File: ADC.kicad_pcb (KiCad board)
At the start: 2 copper layers, 195 parts, among them J1 Conn_01x03_Pin, J2 Screw_Terminal_01x02, J3 Screw_Terminal_01x09, SW1 SW_SPDT, U1 ADS1256IDBR, U10 CD4514BM, U11 ADG5412FBCPZ-RL7, U12 ADR421ARMZ, U13 OPA211ID, U14 ADG5412FBCPZ-RL7, U15 OPA211ID, U16 ADG5412FBCPZ-RL7, U17 OPA211ID, U18 CD4072BM, U19 CD4514BM, U2 MCU-STM32F407VET6_LQFP100_, U20 ADG5412FBCPZ-RL7, U21 ADG5412FBCPZ-RL7, U22 ADG5412FBCPZ-RL7, U23 ADG5412FBCPZ-RL7, U24 OPA211ID, U25 OPA211ID, U26 OPA211ID, U27 OPA211ID, U28 CD4043BPWR, U29 TLV1704AIPWR, U3 ADM2483xRW, U30 TLV1704AIPWR, U31 TLV1704AIPWR, U32 CD4072BM, U4 LM2596S-5, U5 DCP010505BP, U6 TLV1704AIPWR, U7 OPA211ID, U8 AMS1117-3.3, U9 ADG5412FBCPZ-RL7, Y1 8MHz, Y2 ABM3B-25.000MHZ-D2Y-T

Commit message: gần xong
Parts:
- moved C19 37.3 mm to (645.7, 485.9), turned to 180 degrees
- moved C18 37.1 mm to (643.7, 485.8), turned to 0 degrees
- moved C13 28.3 mm to (638.3, 485.1), turned to 180 degrees
- moved C17 24.4 mm to (641.1, 486.6), turned to 0 degrees
- moved R14 21.4 mm to (633.0, 485.3)
- moved R16 21.0 mm to (636.1, 485.4)
- moved R15 20.7 mm to (634.2, 485.3), turned to -90 degrees
- moved R17 19.8 mm to (638.4, 486.6), turned to 180 degrees
- moved C33 16.8 mm to (645.8, 470.2), turned to 90 degrees
- moved C31 16.5 mm to (644.4, 470.1), turned to 90 degrees
- moved C30 16.0 mm to (641.3, 464.5), turned to 0 degrees
- moved R11 15.4 mm to (640.5, 470.8)
- moved U1 15.2 mm to (636.7, 478.8), turned to 0 degrees
- moved R23 15.2 mm to (641.2, 461.5), turned to 180 degrees
- moved SW1 14.3 mm to (645.1, 462.2)
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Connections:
- C1 pad 1: +5V -> GND_ISO
- C1 pad 2: GND -> GND_ISO
- C10 pad 1: +5V_ISO -> GND_ISO
- C12 pad 2: GND -> GND_ISO
- C14 pad 1: GND -> GND_ISO
- C14 pad 2: +3.3V -> GND_ISO
- C15 pad 1: GND -> GND_ISO
- C15 pad 2: +3.3V -> GND_ISO
- C16 pad 2: +3.3V -> GND_ISO
- C20 pad 1: +5V -> GND_ISO
- C21 pad 1: +5V -> GND_ISO
- C28 pad 1: GND -> GND_ISO
- C28 pad 2: +3.3V -> GND_ISO
- C29 pad 1: GND -> GND_ISO
- C32 pad 2: GND -> GND_ISO
- C36 pad 2: GND -> GND_ISO
- C37 pad 1: +3.3V -> GND_ISO
- C37 pad 2: GND -> GND_ISO
- C38 pad 1: +3.3V -> GND_ISO
- C38 pad 2: GND -> GND_ISO
- C39 pad 1: +3.3V -> GND_ISO
- C39 pad 2: GND -> GND_ISO
- C4 pad 1: +5V_ISO -> GND_ISO
- C40 pad 1: +5V_ISO -> GND_ISO
- C41 pad 1: +5V_ISO -> GND_ISO
- C42 pad 2: GND -> GND_ISO
- C43 pad 2: GND -> GND_ISO
- C44 pad 1: +5V -> GND_ISO
- C44 pad 2: GND -> GND_ISO
- C7 pad 1: +3.3V -> GND_ISO
- C7 pad 2: GND -> GND_ISO
- C9 pad 1: +5V_ISO -> GND_ISO
- D1 pad 2: GND -> GND_ISO
- D15 pad 2: GND -> GND_ISO
- D17 pad 2: GND -> GND_ISO
- D2 pad 1: GND -> GND_ISO
- D2 pad 2: Net-(D2-A) -> GND_ISO
- D3 pad 2: GND -> GND_ISO
- FB1 pad 2: +3.3V -> GND_ISO
- J2 pad 1: GND -> GND_ISO
- L1 pad 2: +5V -> GND_ISO
- R18 pad 1: +5V_ISO -> GND_ISO
- R19 pad 2: Net-(U3-B) -> GND_ISO
- R2 pad 1: +3.3V -> GND_ISO
- R2 pad 2: Net-(D2-A) -> GND_ISO
- R20 pad 1: Net-(U3-B) -> GND_ISO
- R22 pad 1: Net-(U3-B) -> GND_ISO
- R24 pad 1: +3.3V -> GND_ISO
- R71 pad 1: +3.3V -> GND_ISO
- R72 pad 1: +3.3V -> GND_ISO
- R73 pad 1: +3.3V -> GND_ISO
- R74 pad 2: +3.3V -> GND_ISO
- R79 pad 2: +3.3V -> GND_ISO
- R80 pad 1: +3.3V -> GND_ISO
- R81 pad 1: +3.3V -> GND_ISO
- R82 pad 1: +3.3V -> GND_ISO
- R83 pad 2: +3.3V -> GND_ISO
- R84 pad 2: +3.3V -> GND_ISO
- R85 pad 1: +3.3V -> GND_ISO
- R86 pad 1: +3.3V -> GND_ISO
- R87 pad 1: +3.3V -> GND_ISO
- R88 pad 1: +3.3V -> GND_ISO
- R89 pad 1: +3.3V -> GND_ISO
- R90 pad 1: +3.3V -> GND_ISO
- RV1 pad 2: Net-(U3-B) -> GND_ISO
- U18 pad 14: +3.3V -> GND_ISO
- U19 pad 24: +3.3V -> GND_ISO
- U2 pad 10: GND -> GND_ISO
- U2 pad 100: GND -> GND_ISO
- U2 pad 11: +3.3V -> GND_ISO
- U2 pad 19: +3.3V -> GND_ISO
- U2 pad 20: GND -> GND_ISO
- U2 pad 27: GND -> GND_ISO
- U2 pad 28: +3.3V -> GND_ISO
- U2 pad 50: +3.3V -> GND_ISO
- U2 pad 75: +3.3V -> GND_ISO
- U2 pad 99: GND -> GND_ISO
- U21 pad 17: GND -> GND_ISO
- U21 pad 3: GND -> GND_ISO
- U21 pad 4: GND -> GND_ISO
- U3 pad 1: +3.3V -> GND_ISO
- U3 pad 13: Net-(U3-B) -> GND_ISO
- U3 pad 14: unconnected-(U3-NC-Pad14) -> GND_ISO
- U3 pad 16: +5V_ISO -> GND_ISO
- U3 pad 2: GND -> GND_ISO
- U3 pad 7: +3.3V -> GND_ISO
- U3 pad 8: GND -> GND_ISO
- U32 pad 14: +3.3V -> GND_ISO
- U4 pad 3: GND -> GND_ISO
- U4 pad 4: +5V -> GND_ISO
- U4 pad 5: GND -> GND_ISO
- U4 pad 6: (no net) -> GND_ISO
- U5 pad 1: +5V -> GND_ISO
- U5 pad 2: GND -> GND_ISO
- U5 pad 6: +5V_ISO -> GND_ISO
- U5 pad 7: unconnected-(U5-NC-Pad7) -> GND_ISO
- U8 pad 1: GND -> GND_ISO
- U8 pad 2: +3.3V -> GND_ISO
- U8 pad 3: +5V -> GND_ISO
- Y2 pad 4: GND -> GND_ISO
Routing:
- net +3.3V: track 9.18 -> 110.1 mm, vias 1 -> 6
- net GND: track 337.3 -> 438.0 mm, vias 25 -> 33
- net DRDY: track 0.00 -> 34.1 mm
- net ADC_RESET: track 0.72 -> 34.0 mm
- net GND_ISO: track 962.3 -> 929.2 mm, vias 33 -> 35
- net SPI3_MISO: track 0.00 -> 32.9 mm
- net CS: track 0.69 -> 27.5 mm
- net Net-(U1-XTAL1/CLKIN): track 0.03 -> 22.8 mm
- net SPI3_MOSI: track 0.00 -> 21.3 mm
- net SPI3_SCK: track 0.30 -> 21.3 mm
- net /VREFN: track 5.79 -> 23.3 mm, vias 0 -> 2
- net Net-(U2-NRST): track 9.79 -> 25.9 mm, vias 0 -> 2
- net /VREFP: track 5.13 -> 20.8 mm, vias 0 -> 2
- net Net-(U3-B): track 15.6 -> 0.00 mm, vias 2 -> 0
- net /AIN7: track 18.0 -> 3.74 mm
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
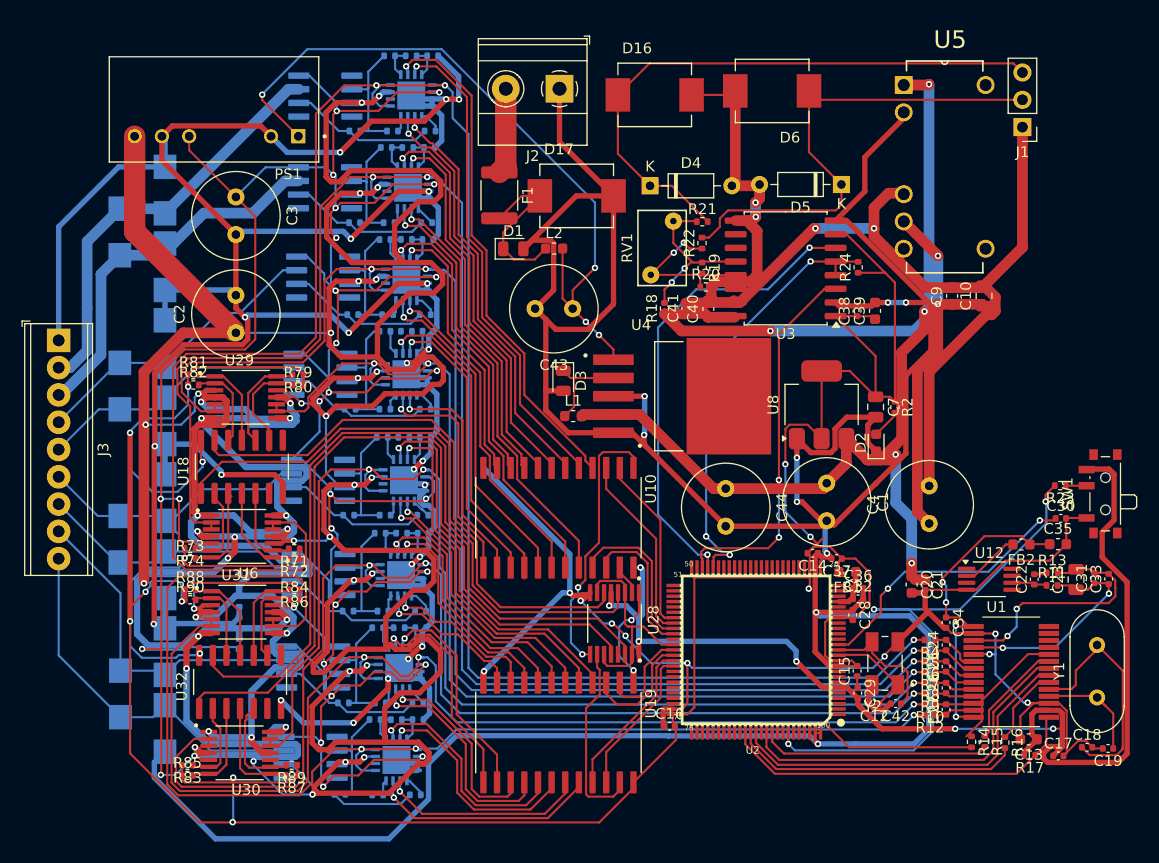
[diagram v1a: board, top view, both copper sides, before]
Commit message: sửa lại dây kích cỡ cũ
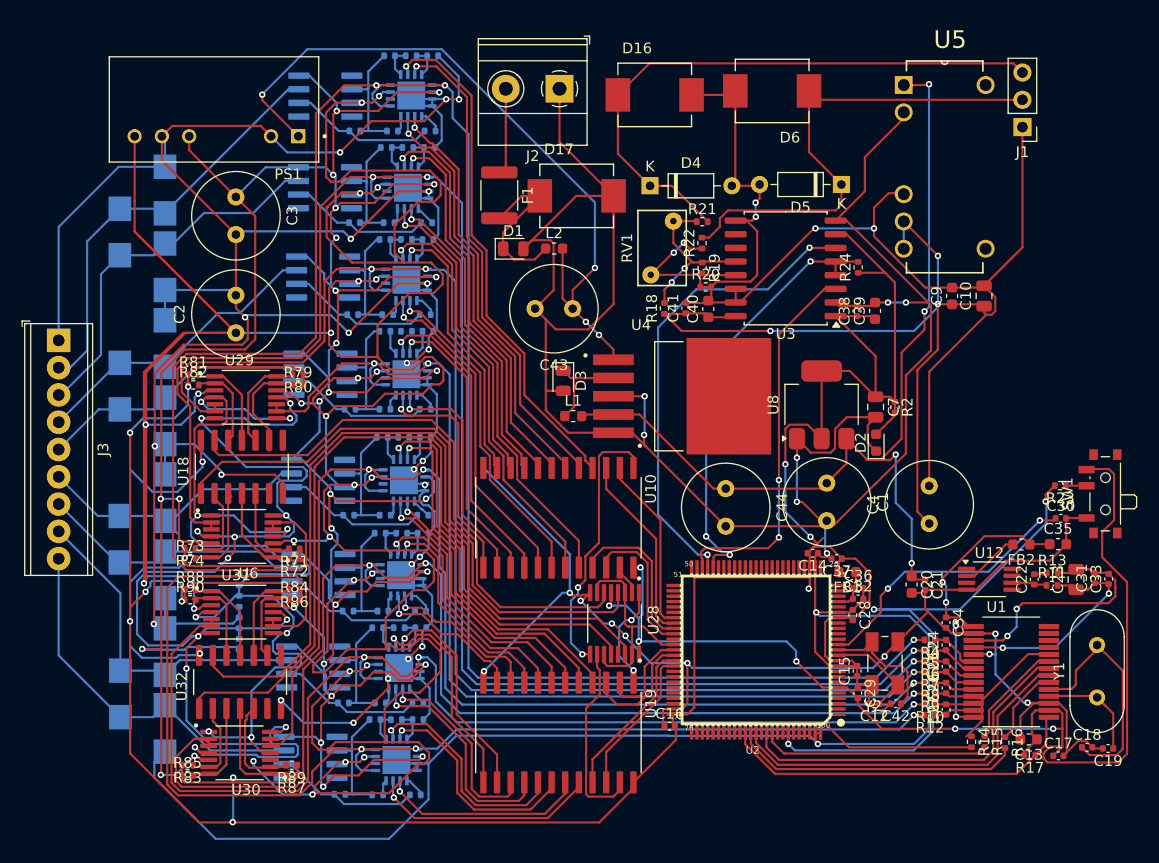
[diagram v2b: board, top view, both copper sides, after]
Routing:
- net GND_ISO: track 929.2 -> 939.1 mm

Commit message: tăng kích cỡ dây
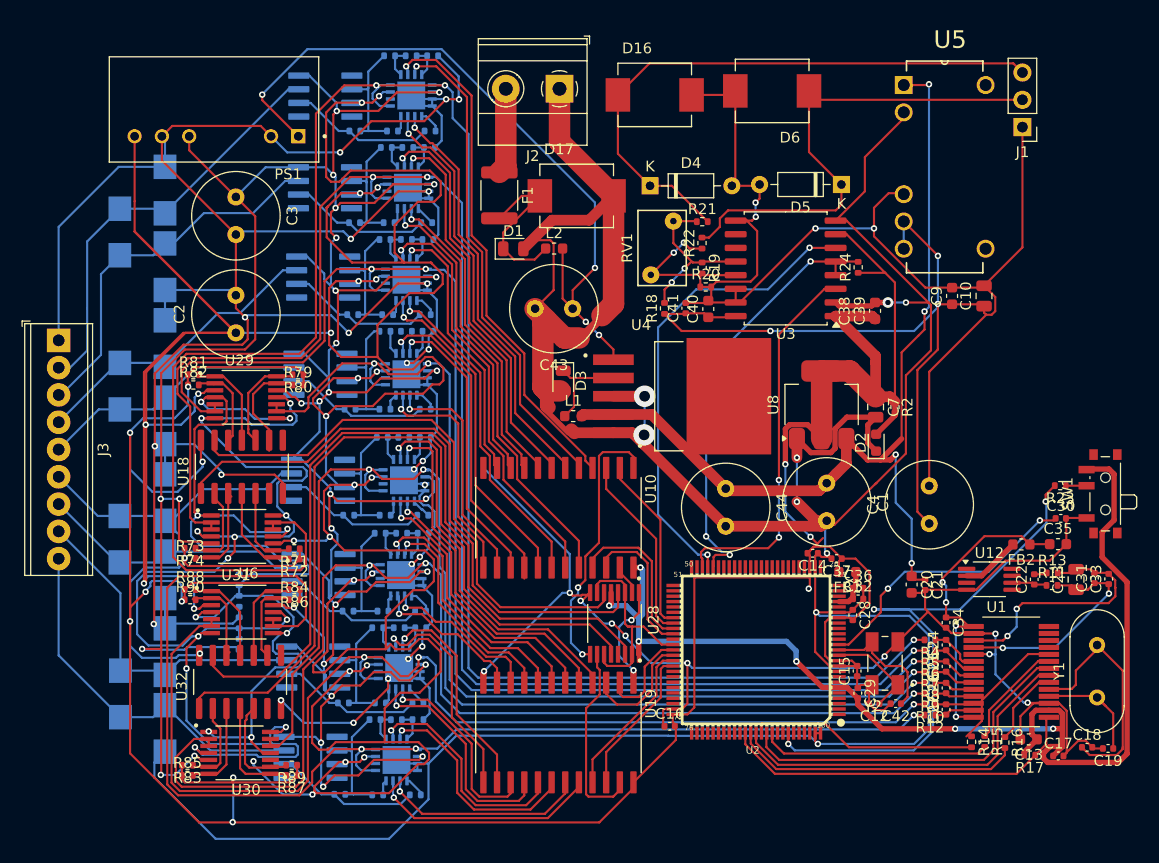
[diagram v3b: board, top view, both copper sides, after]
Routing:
- net GND_ISO: track 939.1 -> 1008.8 mm
